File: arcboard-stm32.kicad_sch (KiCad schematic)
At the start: 87 parts, among them J1 Conn_01x04_Socket, J10 Conn_01x04_Socket, J11 Conn_01x02_Socket, J12 Conn_01x03_Socket, J13 FFC05001-12SBA124W5M, J14 FFC05001-12SBA124W5M, J15 FFC05001-12SBA124W5M, J16 FFC05001-12SBA124W5M, J2 Conn_01x04_Socket, J3 FFC05001-12SBA124W5M, J4 FFC05001-12SBA124W5M, J5 Conn_01x02_Socket, J6 FFC05001-12SBA124W5M, J7 FFC05001-12SBA124W5M, J8 FFC05001-12SBA124W5M, J9 Conn_01x03_Socket, U1 XC6210B332MR-G, U10 1N4148W_C81598, U11 W25Q16JVSSIQTR, U12 TYPE-C-31-M-13, U13 2N7002, U15 TS-1187A-B-A-B, U2 TYPE-C-31-M-13, U3 STM32F405RGTx, U4 2N7002, U5 BAV70S,115, U6 BAV70S,115, U7 BAV70S,115, U8 BAV70S,115, U9 BAV70S,115, Y1 Crystal_GND24

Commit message: silkscreen updates
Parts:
- removed U11: W25Q16JVSSIQTR, kicad-libraries:SOIC-8_L5.3-W5.3-P1.27-LS8.0-BL, symbol kicad-libraries:W25Q16JVSSIQTR
- removed U12: TYPE-C-31-M-13, kicad-libraries:USB-C_SMD-TYPE-C-31-M-12, symbol kicad-libraries:TYPE-C-31-M-13
- added LOGO1, LOGO2: **REF, kicad-libraries:awesome-logo, symbol kicad-libraries:awesome-logo
- added LOGO3: **REF, kicad-libraries:cyboard-logo-10mm, symbol kicad-libraries:cyboard-logo-10mm
- added LOGO4: **REF, kicad-libraries:qmk-lite, symbol kicad-libraries:qmk-lite-logo
- added U14: W25Q128JVSIQTR, kicad-libraries:SOIC-8_L5.3-W5.3-P1.27-LS8.0-BL, symbol kicad-libraries:W25Q128JVSIQTR
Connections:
- net +3V3: now also U14.3 (IO2), U14.7 (IO3), U14.8 (VCC)
- net FLASH_CS: now also U14.1 (CS#)
- net GND: now also U14.4 (GND)
- net SPI1_CLK: now also U14.6 (CLK)
- net SPI1_MISO: now also U14.2 (DO)
- net SPI1_MOSI: now also U14.5 (DI)
- no-connect marks 42 -> 37

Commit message: silkscreen improvements
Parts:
- added LOGO5: **REF, kicad-libraries:arcboard-stm32-qr-code-10x10, symbol kicad-libraries:qmk-lite-logo
- added LOGO6: **REF, kicad-libraries:cyboard-logo-5mm, symbol kicad-libraries:qmk-lite-logo
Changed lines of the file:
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@@
 	)
 	(symbol
+		(lib_id "kicad-libraries:qmk-lite-logo")
+		(at 491.49 447.04 0)
+		(unit 1)
+		(exclude_from_sim no)
+		(in_bom no)
+		(on_board yes)
+		(dnp no)
+		(fields_autoplaced yes)
+		(property "Reference" "LOGO6"
+			(at 494.03 445.7699 0)
+			(effects
+				(font
+					(size 1.27 1.27)
+				)
+				(justify left)
+			)
+		)
+		(property "Value" "**REF"
+			(at 494.03 448.3099 0)
+			(effects
+				(font
+					(size 1.27 1.27)
+				)
+				(justify left)
+			)
+		)
+		(property "Footprint" "kicad-libraries:cyboard-logo-5mm"
+			(at 491.49 447.04 0)
+			(effects
+				(font
+					(size 1.27 1.27)
+				)
+				(hide yes)
+			)
+		)
+		(property "Datasheet" ""
+			(at 491.49 447.04 0)
+			(effects
+				(font
+					(size 1.27 1.27)
+				)
+				(hide yes)
+			)
+		)
+		(property "Description" "cyboard logo 5mm"
+			(at 491.49 447.04 0)
+			(effects
+				(font
+					(size 1.27 1.27)
+				)
+				(hide yes)
+			)
+		)
+		(instances
+			(project "arcboard-stm32"
+				(path "/77409937-8008-4619-ae71-6a56c8773006"
+					(reference "LOGO6")
+					(unit 1)
+				)
+			)
+		)
+	)
+	(symbol
 		(lib_id "power:+3V3")
 		(at 356.87 377.19 180)
@@
 					(unit 1)
 				)
+			)
+		)
+	)
+	(symbol
+		(lib_id "kicad-libraries:qmk-lite-logo")
+		(at 491.49 441.96 0)
+		(unit 1)
+		(exclude_from_sim no)
+		(in_bom no)
+		(on_board yes)
+		(dnp no)
+		(fields_autoplaced yes)
+		(property "Reference" "LOGO5"
+			(at 494.03 440.6899 0)
+			(effects
+				(font
+					(size 1.27 1.27)
+				)
+				(justify left)
+			)
+		)
+		(property "Value" "**REF"
+			(at 494.03 443.2299 0)
+			(effects
+				(font
+					(size 1.27 1.27)
+				)
+				(justify left)
+			)
+		)
+		(property "Footprint" "kicad-libraries:arcboard-stm32-qr-code-10x10"
+			(at 491.49 441.96 0)
+			(effects
+				(font
+					(size 1.27 1.27)
+				)
+				(hide yes)
+			)
+		)
+		(property "Datasheet" ""
+			(at 491.49 441.96 0)
+			(effects
+				(font
+					(size 1.27 1.27)
+				)
+				(hide yes)
+			)
+		)
+		(property "Description" "arcboard-stm32 repo qr code"
+			(at 491.49 441.96 0)
+			(effects
+				(font
+					(size 1.27 1.27)
+				)
+				(hide yes)
+			)
+		)
+		(instances
+			(project "arcboard-stm32"
+				(path "/77409937-8008-4619-ae71-6a56c8773006"
+					(reference "LOGO5")
+					(unit 1)
+				)

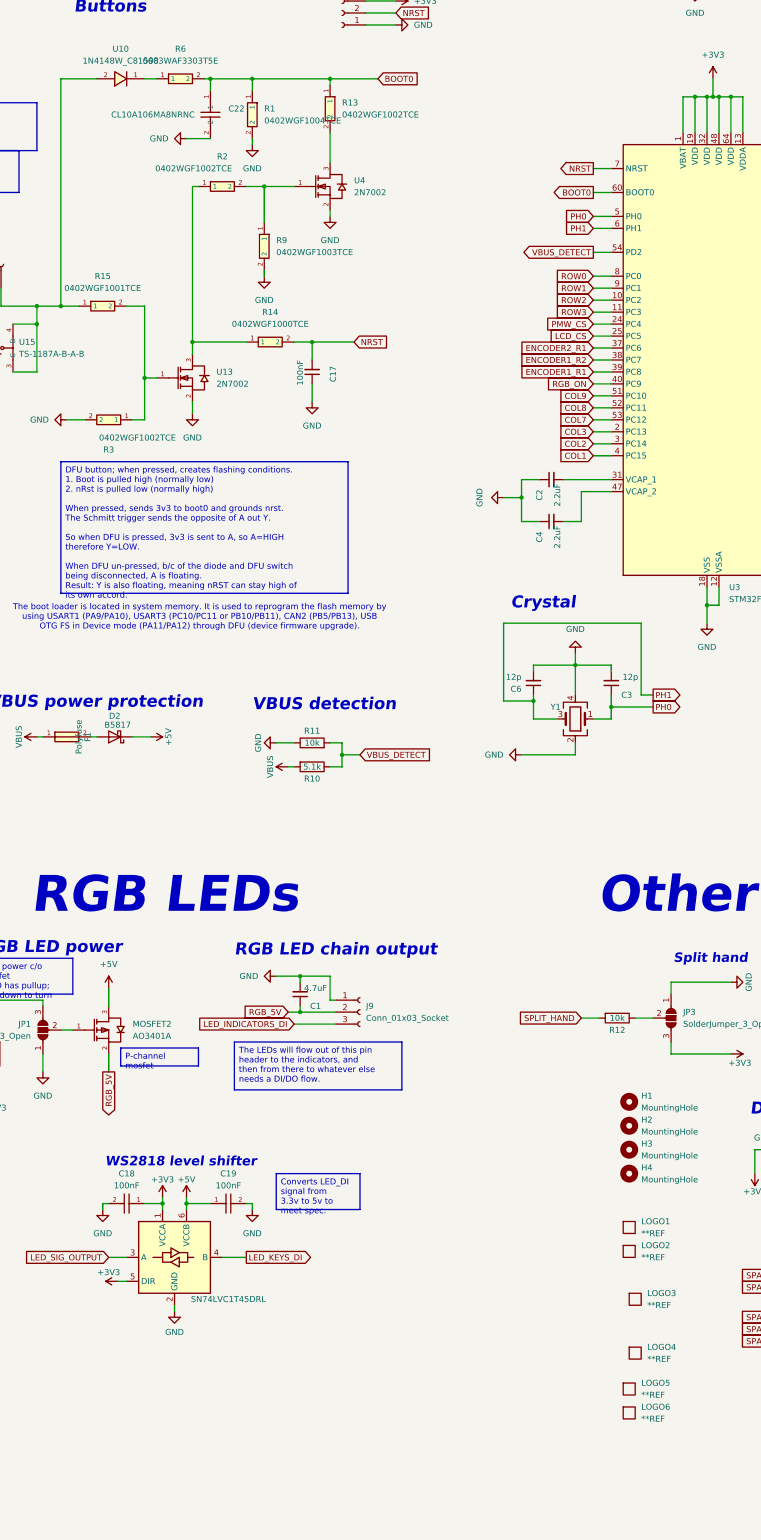
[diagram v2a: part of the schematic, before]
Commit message: moved a few items, silkscreen improvements
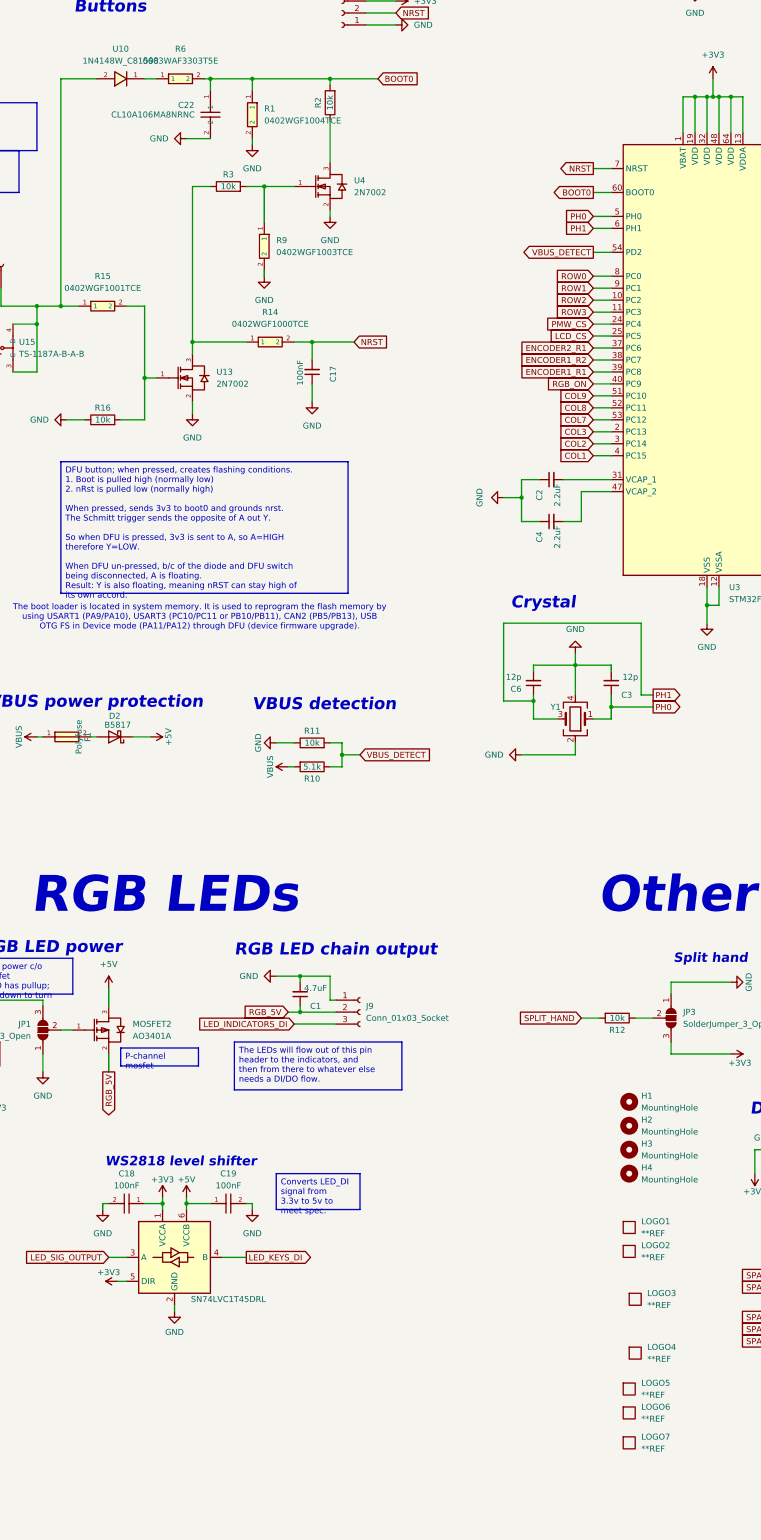
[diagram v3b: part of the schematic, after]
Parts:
- removed R13, R2, R3: 0402WGF1002TCE, Resistor_SMD:R_0402_1005Metric, symbol kicad-libraries:0402WGF1002TCE
- added LOGO7: **REF, kicad-libraries:awesome-logo-25mm, symbol kicad-libraries:qmk-lite-logo
- added R16, R2, R3: 10k, Resistor_SMD:R_0402_1005Metric, symbol Device:R
- J1, J10, J11, J12: now left out of the parts list
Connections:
- net BOOT0: now also R2.2
- net GND: now also R16.1
- net at R9.1, U4.1 (G): now also R3.2
- net at U4.3 (D): now also R2.1
- net at R15.2, U13.1 (G): now also R16.2
- net at R14.1, U13.3 (D): now also R3.1

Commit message: production version
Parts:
- removed R4, R5: 5.1k, Resistor_SMD:R_0402_1005Metric, symbol Device:R
- removed U2: TYPE-C-31-M-13, kicad-libraries:USB-C_SMD-TYPE-C-31-M-12, symbol kicad-libraries:TYPE-C-31-M-13
- added J17: Conn_01x04_Socket, Connector_JST:JST_XH_S4B-XH-A_1x04_P2.50mm_Horizontal, symbol Connector:Conn_01x04_Socket
- C22: footprint Capacitor_SMD:C_0201_0603Metric -> kicad-libraries:C0603
- R6: footprint Resistor_SMD:R_0201_0603Metric -> kicad-libraries:R0603
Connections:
- net GND: now also J17.1 (Pin_1)
- net USB_CONN_DM: now also J17.2 (Pin_2)
- net USB_CONN_DP: now also J17.3 (Pin_3)
- net VBUS: now also J17.4 (Pin_4)
- no-connect marks 37 -> 34
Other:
- note added: "Power"
- note added: "SPI External flash"
- note added: "Serial ESD"
- note added: "Serial VBUS"
- note added: "Serial port pins"
- note added: "Spare pins"
- note added: "USB connector breakout"
- note removed: "Serial-TRRS ESD"
- note removed: "Serial_VBUS"
- note removed: "USB-C connector"
- moved on the sheet: C1, C10, C11, C12, C13, C14, C15, C17, C18, C19, C2, C20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

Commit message: fixing bad mosfet configuration, changing crystal to 12mhz
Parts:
- Y1: LCSC C518154 -> C9002
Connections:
- net +3V3: now also MOSFET3.2 (S); no longer MOSFET3.3 (D)
- net +5V: now also MOSFET2.2 (S); no longer MOSFET2.3 (D)
- net LCD_3V3: now also MOSFET3.3 (D); no longer MOSFET3.2 (S)
- net RGB_5V: now also MOSFET2.3 (D); no longer MOSFET2.2 (S)
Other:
- note added: "v1.1: Moved from 8mhz to 12mhz crystal, to satisfy QMK defaults."
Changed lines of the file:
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@@
 		)
 	)
+	(text "v1.1: Moved from 8mhz to 12mhz crystal, to satisfy QMK defaults."
+		(exclude_from_sim no)
+		(at 481.076 278.384 0)
+		(effects
+			(font
+				(size 1.27 1.27)
+			)
+		)
+	)
 	(text "PAD2/3\nCOL9/10"
 		(exclude_from_sim no)
@@
 	(wire
 		(pts
-			(xy 566.42 326.39) (xy 566.42 330.2)
-		)
-		(stroke
-			(width 0)
-			(type default)
-		)
-	)
-	(wire
-		(pts
 			(xy 601.98 323.85) (xy 607.06 323.85)
 		)
@@
 	(wire
 		(pts
+			(xy 566.42 328.93) (xy 566.42 330.2)
+		)
+		(stroke
+			(width 0)
+			(type default)
+		)
+	)
+	(wire
+		(pts
 			(xy 166.37 232.41) (xy 179.07 232.41)
 		)
@@
 		)
 	)
+	(global_label "RGB_5V"
+		(shape output)
+		(at 566.42 328.93 90)
+		(fields_autoplaced yes)
+		(effects
+			(font
+				(size 1.27 1.27)
+			)
+			(justify left)
+		)
+		(property "Intersheetrefs" "${INTERSHEET_REFS}"
+			(at 566.42 318.8691 90)
+			(effects
+				(font
+					(size 1.27 1.27)
+				)
+				(justify left)
+				(hide yes)
+			)
+		)
+	)
 	(global_label "SERIAL_CONN_RX"
 		(shape bidirectional)
@@
 		)
 	)
-	(global_label "LCD_3V3"
-		(shape output)
-		(at 88.9 345.44 270)
-		(fields_autoplaced yes)
-		(effects
-			(font
-				(size 1.27 1.27)
-			)
-			(justify right)
-		)
-		(property "Intersheetrefs" "${INTERSHEET_REFS}"
-			(at 88.9 356.4685 90)
-			(effects
-				(font
-					(size 1.27 1.27)
-				)
-				(justify right)
-				(hide yes)
-			)
-		)
-	)
 	(global_label "COL4"
 		(shape output)
@@
 		)
 	)
-	(global_label "RGB_5V"
-		(shape output)
-		(at 566.42 344.17 270)
-		(fields_autoplaced yes)
-		(effects
-			(font
-				(size 1.27 1.27)
-			)
-			(justify right)
-		)
-		(property "Intersheetrefs" "${INTERSHEET_REFS}"
-			(at 566.42 354.2309 90)
-			(effects
-				(font
-					(size 1.27 1.27)
-				)
-				(justify right)
-				(hide yes)
-			)
-		)
-	)
 	(global_label "SPI1_MOSI"
 		(shape input)
@@
 		)
 	)
+	(global_label "LCD_3V3"
+		(shape output)
+		(at 88.9 327.66 90)
+		(fields_autoplaced yes)
+		(effects
+			(font
+				(size 1.27 1.27)
+			)
+			(justify left)
+		)
+		(property "Intersheetrefs" "${INTERSHEET_REFS}"
+			(at 88.9 316.6315 90)
+			(effects
+				(font
+					(size 1.27 1.27)
+				)
+				(justify left)
+				(hide yes)
+			)
+		)
+	)
 	(global_label "ROW5"
 		(shape input)
@@
 	(symbol
 		(lib_id "power:+3V3")
-		(at 88.9 327.66 0)
+		(at 88.9 345.44 180)
 		(unit 1)
 		(exclude_from_sim no)
@@
 		(fields_autoplaced yes)
 		(property "Reference" "#PWR083"
-			(at 88.9 331.47 0)
+			(at 88.9 341.63 0)
 			(effects
 				(font
@@
 		)
 		(property "Value" "+3V3"
-			(at 88.9 322.58 0)
+			(at 91.44 346.7099 0)
 			(effects
 				(font
 					(size 1.27 1.27)
 				)
+				(justify right)
 			)
 		)
 		(property "Footprint" ""
-			(at 88.9 327.66 0)
+			(at 88.9 345.44 0)
 			(effects
 				(font
@@
 		)
 		(property "Datasheet" ""
-			(at 88.9 327.66 0)
+			(at 88.9 345.44 0)
 			(effects
 				(font
@@
 		)
 		(property "Description" "Power symbol creates a global label with name \"+3V3\""
-			(at 88.9 327.66 0)
+			(at 88.9 345.44 0)
 			(effects
 				(font
@@
 			)
 		)
-		(property "Datasheet" "https://datasheet.lcsc.com/lcsc/2006031009_Suzhou-Liming-Elec-3225-8-00-10-10-10-A_C518154.pdf"
+		(property "Datasheet" "https://jlcpcb.com/api/file/downloadByFileSystemAccessId/8588879072109322240"
 			(at 480.06 266.7 0)
 			(effects
@@
 			)
 		)
-		(property "LCSC" "C518154"
+		(property "LCSC" "C9002"
 			(at 480.06 266.7 0)
 			(effects
@@
 		(lib_name "+5V_4")
 		(lib_id "power:+5V")
-		(at 566.42 326.39 0)
+		(at 566.42 344.17 180)
 		(unit 1)
 		(exclude_from_sim no)
@@
 		(fields_autoplaced yes)
 		(property "Reference" "#PWR021"
-			(at 566.42 330.2 0)
+			(at 566.42 340.36 0)
 			(effects
 				(font
@@
 		)
 		(property "Value" "+5V"
-			(at 566.42 321.31 0)
+			(at 568.96 345.4399 0)
 			(effects
 				(font
 					(size 1.27 1.27)
 				)
+				(justify right)
 			)
 		)
 		(property "Footprint" ""
-			(at 566.42 326.39 0)
+			(at 566.42 344.17 0)
 			(effects
 				(font
@@
 		)
 		(property "Datasheet" ""
-			(at 566.42 326.39 0)
+			(at 566.42 344.17 0)
 			(effects
 				(font
@@
 		)
 		(property "Description" "Power symbol creates a global label with name \"+5V\""
-			(at 566.42 326.39 0)
+			(at 566.42 344.17 0)
 			(effects
 				(font
@@
 		)
 		(instances
-			(project ""
+			(project "arcboard-stm32"
 				(path "/77409937-8008-4619-ae71-6a56c8773006"
 					(reference "#PWR021")
